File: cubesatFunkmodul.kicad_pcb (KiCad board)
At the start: 4 copper layers, 85 x 85 mm, 101 parts, among them CON11 DISCO-CON, CON12 DISCO-CON, Q1 MMBT5401-TP, Q2 AO3414, Q3 MMBT5551-TP, Q4 MMBT5551-TP, Q5 MMBT5551-TP, Q6 MMBT5551-TP, Q7 MMBT5551-TP, Q8 MMBT5551-TP, U1 MC74HC4538A, U2 MAX892, U3 ATMEGA128-16AU, U4 LTC3113, U5 RFM23BP, Y1 Crystal_GND24

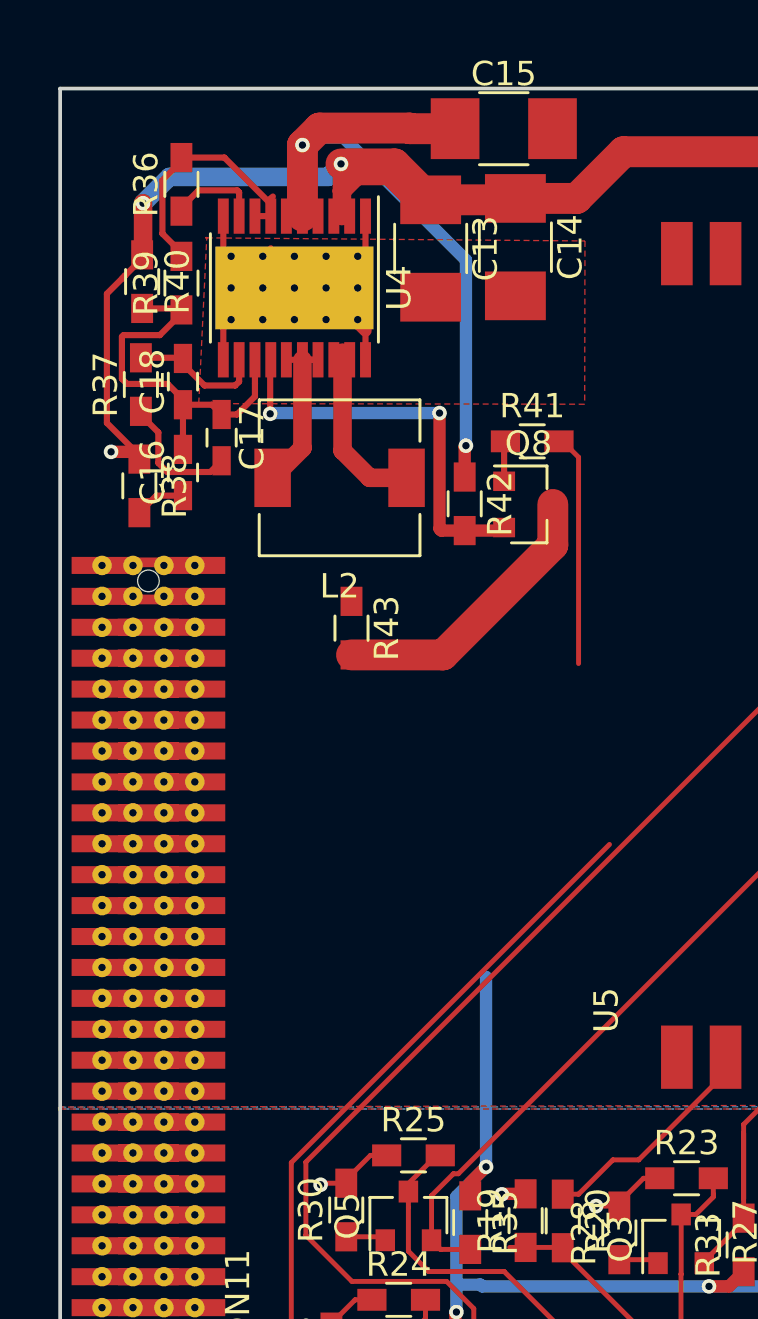
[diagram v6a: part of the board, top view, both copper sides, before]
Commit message: Resolves Bug in Cubesat Connector Library
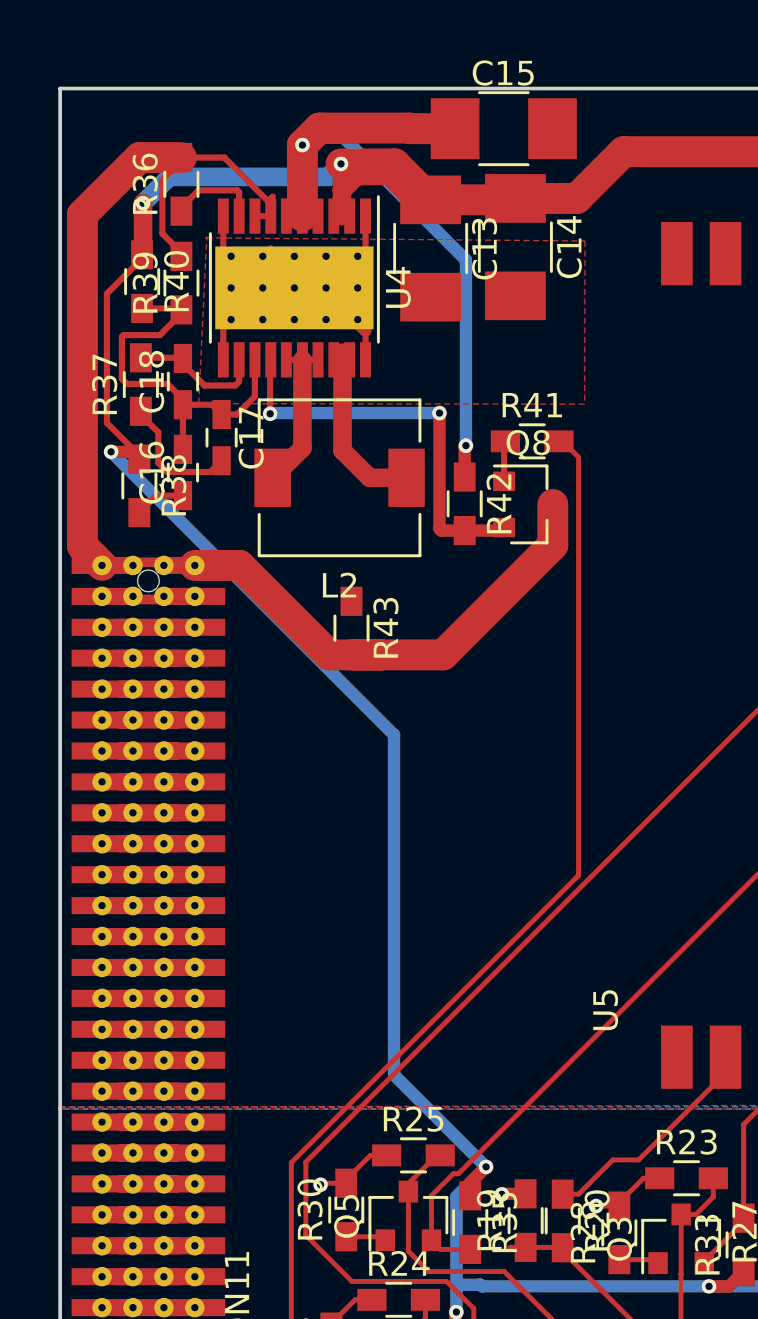
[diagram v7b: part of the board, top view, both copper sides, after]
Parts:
- Q1: value MMBT5401-TP -> SSM3J334RLFTR-ND
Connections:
- CON11 pad 12: Net-(CON11-Pad11) -> Net-(CON11-Pad12)
- CON11 pad 14: Net-(CON11-Pad13) -> Net-(CON11-Pad14)
- CON11 pad 15: Net-(CON11-Pad135) -> Net-(CON11-Pad15)
- CON11 pad 16: Net-(CON11-Pad135) -> Net-(CON11-Pad16)
- CON11 pad 17: Net-(CON11-Pad137) -> Net-(CON11-Pad17)
- CON11 pad 18: Net-(CON11-Pad137) -> Net-(CON11-Pad18)
- CON11 pad 19: Net-(CON11-Pad139) -> Net-(CON11-Pad19)
- CON11 pad 2: GND -> Net-(CON11-Pad2)
- CON11 pad 20: Net-(CON11-Pad139) -> Net-(CON11-Pad20)
- CON11 pad 21: Net-(CON11-Pad141) -> Net-(CON11-Pad21)
- CON11 pad 22: Net-(CON11-Pad141) -> Net-(CON11-Pad22)
- CON11 pad 23: Net-(CON11-Pad143) -> Net-(CON11-Pad23)
- CON11 pad 24: Net-(CON11-Pad143) -> Net-(CON11-Pad24)
- CON11 pad 25: Net-(CON11-Pad145) -> Net-(CON11-Pad25)
- CON11 pad 26: Net-(CON11-Pad145) -> Net-(CON11-Pad26)
- CON11 pad 27: Net-(CON11-Pad147) -> Net-(CON11-Pad27)
- CON11 pad 28: Net-(CON11-Pad147) -> Net-(CON11-Pad28)
- CON11 pad 29: Net-(CON11-Pad149) -> Net-(CON11-Pad29)
- CON11 pad 3: Net-(CON11-Pad123) -> Net-(CON11-Pad3)
- CON11 pad 30: Net-(CON11-Pad149) -> GND
- CON11 pad 4: Net-(CON11-Pad123) -> Net-(CON11-Pad4)
- CON11 pad 5: Net-(CON11-Pad125) -> Net-(CON11-Pad5)
- CON11 pad 6: Net-(CON11-Pad125) -> Net-(CON11-Pad6)
- CON11 pad 7: Net-(CON11-Pad127) -> Net-(CON11-Pad7)
- CON11 pad 8: Net-(CON11-Pad127) -> Net-(CON11-Pad8)
- CON11 pad 9: Net-(CON11-Pad10) -> Net-(CON11-Pad9)
- Q1 pad 1: Net-(D1-Pad1) -> Net-(D3-Pad1)
- Q1 pad 2: Net-(D3-Pad1) -> Net-(D1-Pad1)
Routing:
- net GND: track 67.0 -> 96.0 mm
- net /Funkmodul1/Funkeinheit/5V: track 100.5 -> 128.4 mm
- net Net-(D1-Pad1): track 3.34 -> 11.1 mm
- net Net-(D3-Pad1): track 37.0 -> 29.2 mm
- net /Funkmodul1/~ON~: track 93.3 -> 100.3 mm

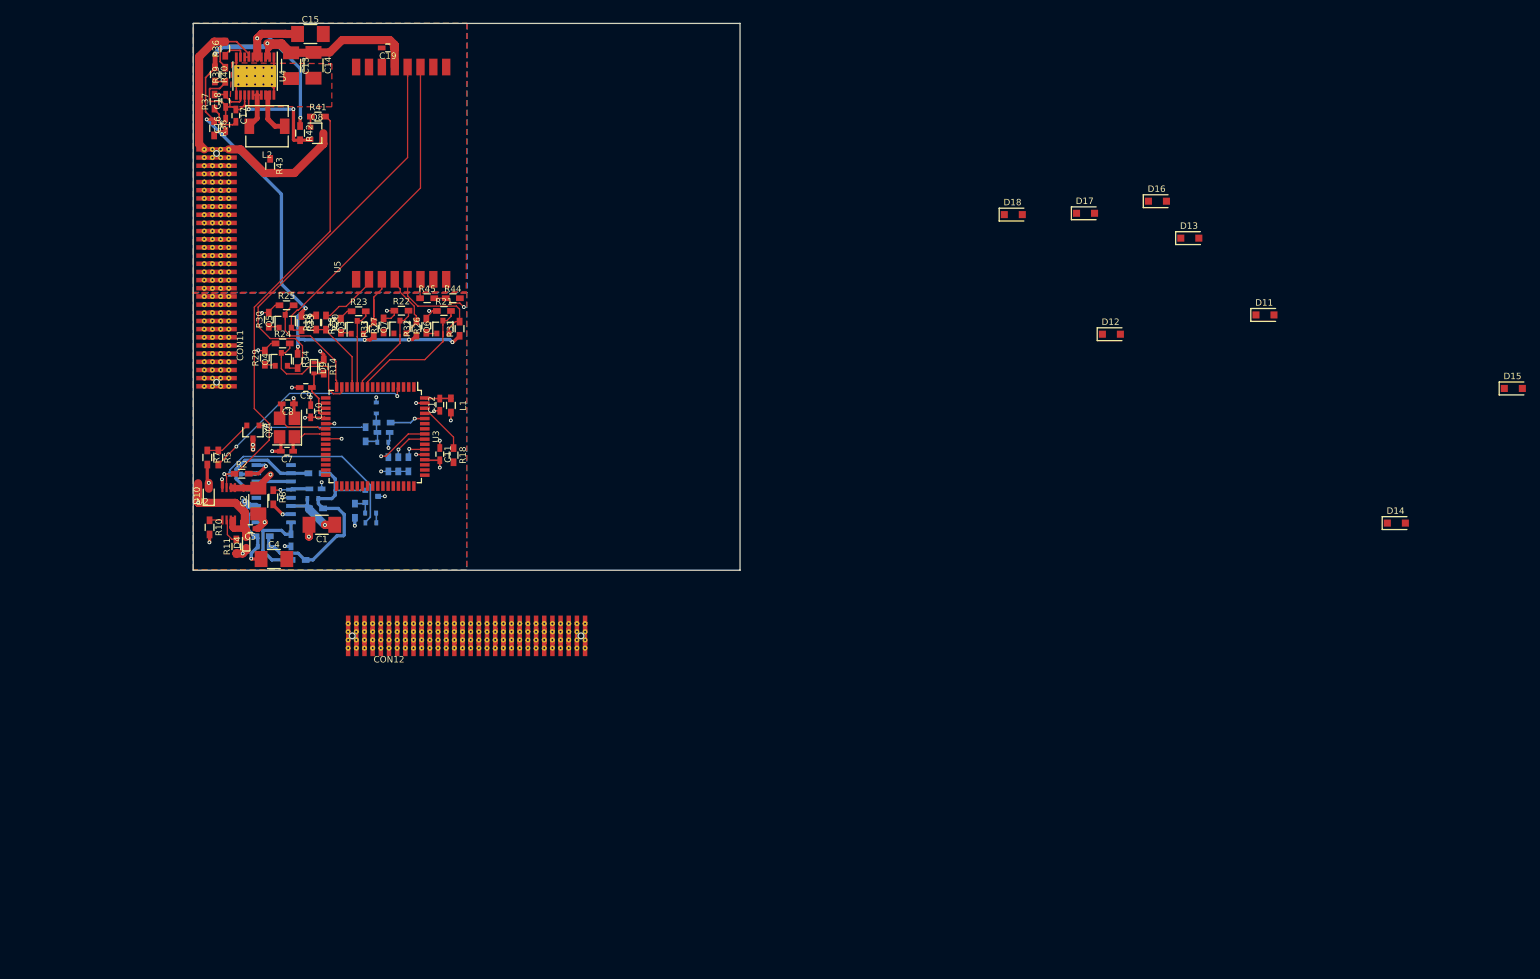
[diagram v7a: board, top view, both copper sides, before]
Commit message: Integrates Connectors in Design
Beginn to add mounting holes
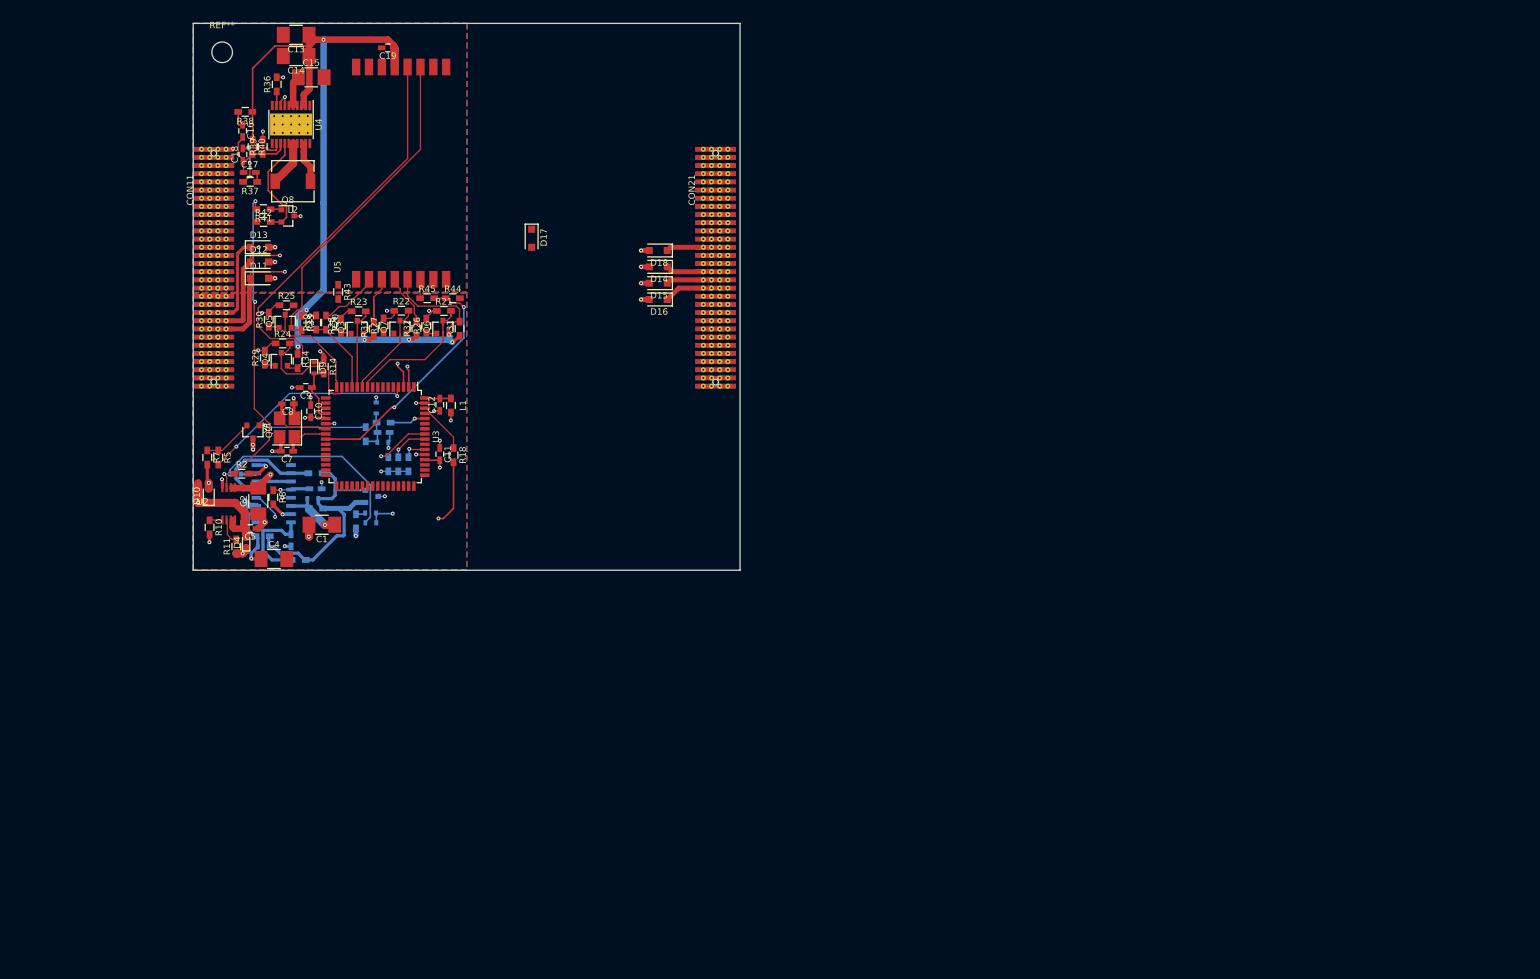
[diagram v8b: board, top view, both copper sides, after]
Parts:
- removed CON12: DISCO-CON, cubesatFunkmodul:Cubesatconnector
- added CON21: DISCO-CON2, cubesatFunkmodul:Cubesatconnector, F.Cu at (132.3, 72.0)
- added REF**: MountingHole_3.2mm_M3, Mounting_Holes:MountingHole_3.2mm_M3, F.Cu at (55.5, 38.5)
- CON11: value DISCO-CON -> DISCO-CON1
- moved D11 156.4 mm to (61.3, 73.6)
- moved D13 144.6 mm to (61.3, 68.8)
- moved D15 133.9 mm to (123.3, 74.4), turned to 180 degrees
- moved D12 132.9 mm to (61.3, 71.1)
- moved D14 121.4 mm to (123.3, 71.8), turned to 180 degrees
- moved D17 86.2 mm to (103.6, 67.4), turned to 270 degrees
- moved D16 79.1 mm to (123.3, 76.9), turned to 180 degrees
- moved D18 55.5 mm to (123.3, 69.3), turned to 180 degrees
- moved R43 22.2 mm to (73.5, 75.7)
- moved R41 16.7 mm to (61.9, 62.9), turned to 180 degrees
- moved R42 14.9 mm to (61.9, 64.9), turned to 0 degrees
- moved R37 13.6 mm to (59.8, 58.6), turned to 180 degrees
- moved Q8 13.6 mm to (65.7, 63.9)
- moved R40 12.7 mm to (60.2, 53.2)
- moved R39 12.6 mm to (61.8, 53.2)
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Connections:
- net /Funkmodul1/TCK renamed /Connector/TCK
- net /Funkmodul1/TMS renamed /Connector/TMS
- CON11 pad 21: Net-(CON11-Pad21) -> /Connector/~ENABLE1~
- CON11 pad 22: Net-(CON11-Pad22) -> /Funkmodul1/TX
- CON11 pad 23: Net-(CON11-Pad23) -> /Funkmodul1/RX
- CON11 pad 8: Net-(CON11-Pad8) -> /Connector/3.3V
- D14 pad 1: (no net) -> /Connector/RX2
- D15 pad 1: (no net) -> /Connector/TX2
- D16 pad 1: (no net) -> /Connector/~ENABLE2~
- U3 pad 5: (no net) -> /Connector/~RBF~
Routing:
- net /Connector/~ENABLE1~: track 1.52 -> 68.5 mm, vias 0 -> 2
- net /Connector/3.3V: track 53.5 -> 104.8 mm
- net /Funkmodul1/TX: track 0.00 -> 50.4 mm, vias 0 -> 2
- net /Funkmodul1/Funkeinheit/5V: track 128.4 -> 177.5 mm, vias 8 -> 6
- net /Funkmodul1/RX: track 0.00 -> 47.3 mm, vias 0 -> 2
- net /Funkmodul1/WDG_TRIGGER: track 0.00 -> 40.1 mm, vias 0 -> 2
- net GND: track 96.0 -> 58.3 mm, vias 22 -> 33
- net VBAT: track 29.0 -> 6.02 mm, vias 2 -> 0
- net /Funkmodul1/Funkeinheit/PGND: track 18.7 -> 0.00 mm
- net /Funkmodul1/~ON~: track 100.3 -> 83.4 mm, vias 1 -> 3
- net Net-(C18-Pad2): track 5.60 -> 13.0 mm, vias 0 -> 2
- net Net-(D3-Pad1): track 29.2 -> 36.2 mm
- net /Connector/~ENABLE2~: track 0.00 -> 6.35 mm
- net /Connector/RX2: track 0.00 -> 5.92 mm
- net /Connector/TX2: track 0.00 -> 5.82 mm
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- removed copper zone on In1.Cu, net /Funkmodul1/Funkeinheit/PGND
